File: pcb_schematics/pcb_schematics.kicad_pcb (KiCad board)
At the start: 2 copper layers, 140 x 108 mm, 56 parts, among them J1 CUE_SJ1-352XNG, J2 Conn_01x01_Pin, SW1 SW_Push, SW2 SW_Push, SW3 SW_Push, SW4 SW_Push, SW5 RotaryEncoder, SW6 RotaryEncoder, U1 RPi_Pico_TH, U2 RDA5807M_Module, U3 LM386, U4 LM386

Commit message: Pcb (#1)
* Converted to connectors

* Updates PCb according to ROB's feedback

Added PCb layour according to the discussion with butoons and display on top and display below using front copper. Added Radio module using back copper. Speakers left to set up using back copper.

* compeltes PCB

Only the DRC has a couple errors

* Updates footprints in schematic

* Fixes errors in DRC

Adds SMD capacitors too

* Runs DRC and ERC again

* Accomodating usb cable

* Revision 3

Changed the amplifier and the rotary encoder schemtic. Needs work on pcb

* completes third version of PCB

* fixed issues mentioned by rob and brent

Fix iteration 1

* made changes based on changes requested

Fix iteration 2

* Submitted to JLCPCB

Modification with pcb_schematics being the final version.
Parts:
- removed C17, C18, C19, C20, C21, C22, C23, C24, C25, C26, C27, C28, C29, C30, C31, C32: 10 nF, Capacitor_THT:CP_Radial_D4.0mm_P1.50mm
- removed SW2, SW3, SW4: SW_Push, Button_Switch_THT:Push_E-Switch_KS01Q01
- removed SW5, SW6: RotaryEncoder, Rotary_Encoder:RotaryEncoder_Alps_EC11E-Switch_Vertical_H20mm
- added H1: MountingHole, MountingHole:MountingHole_3.2mm_M3, F.Cu at (100.0, 48.0)
- added H2: MountingHole, MountingHole:MountingHole_3.2mm_M3, F.Cu at (190.0, 48.0)
- added H3: MountingHole, MountingHole:MountingHole_3.2mm_M3, F.Cu at (190.0, 138.0)
- added H4: MountingHole, MountingHole:MountingHole_3.2mm_M3, F.Cu at (100.0, 138.0)
- added J3: Conn_01x05, Connector_PinHeader_2.54mm:PinHeader_1x05_P2.54mm_Vertical, F.Cu at (176.5, 45.3)
- added J4: Conn_01x05, Connector_PinHeader_2.54mm:PinHeader_1x05_P2.54mm_Vertical, F.Cu at (149.0, 45.3)
- added J5: Conn_01x05, Connector_PinHeader_2.54mm:PinHeader_1x05_P2.54mm_Vertical, F.Cu at (123.0, 45.8)
- added R10: 10Ω, Resistor_THT:R_Axial_DIN0207_L6.3mm_D2.5mm_P10.16mm_Horizontal, F.Cu at (177.0, 60.0)
- added R5: 10Ω, Resistor_THT:R_Axial_DIN0207_L6.3mm_D2.5mm_P10.16mm_Horizontal, F.Cu at (156.5, 49.0)
- added R6: 10Ω, Resistor_THT:R_Axial_DIN0207_L6.3mm_D2.5mm_P10.16mm_Horizontal, F.Cu at (140.0, 57.3)
- added R7: 10kΩ, Resistor_THT:R_Axial_DIN0207_L6.3mm_D2.5mm_P10.16mm_Horizontal, F.Cu at (129.0, 55.0)
- added R8: 10kΩ, Resistor_THT:R_Axial_DIN0207_L6.3mm_D2.5mm_P10.16mm_Horizontal, F.Cu at (121.0, 65.0)
- added R9: 10Ω, Resistor_THT:R_Axial_DIN0207_L6.3mm_D2.5mm_P10.16mm_Horizontal, F.Cu at (169.0, 49.0)
- added R_Pullup1: 10kΩ, Resistor_THT:R_Axial_DIN0207_L6.3mm_D2.5mm_P10.16mm_Horizontal, F.Cu at (153.0, 51.0)
- added R_Pullup2: 10kΩ, Resistor_THT:R_Axial_DIN0207_L6.3mm_D2.5mm_P10.16mm_Horizontal, F.Cu at (137.0, 55.0)
- added R_Pullup4: 10kΩ, Resistor_THT:R_Axial_DIN0207_L6.3mm_D2.5mm_P10.16mm_Horizontal, F.Cu at (125.0, 50.0)
- added R_Pullup5: 10kΩ, Resistor_THT:R_Axial_DIN0207_L6.3mm_D2.5mm_P10.16mm_Horizontal, F.Cu at (117.0, 50.0)
- added R_Pullup6: 10kΩ, Resistor_THT:R_Axial_DIN0207_L6.3mm_D2.5mm_P10.16mm_Horizontal, F.Cu at (182.0, 53.0)
- added R_Pullup7: 10kΩ, Resistor_THT:R_Axial_DIN0207_L6.3mm_D2.5mm_P10.16mm_Horizontal, F.Cu at (166.0, 51.0)
- added TP1: TestPoint, TestPoint:TestPoint_Keystone_5000-5004_Miniature, F.Cu at (171.0, 137.0)
- added TP10: TestPoint, TestPoint:TestPoint_Keystone_5000-5004_Miniature, B.Cu at (184.0, 106.3)
- added TP11: TestPoint, TestPoint:TestPoint_Keystone_5000-5004_Miniature, B.Cu at (186.0, 84.0)
- added TP12: TestPoint, TestPoint:TestPoint_Keystone_5000-5004_Miniature, B.Cu at (186.0, 71.0)
- added TP13: TestPoint, TestPoint:TestPoint_Keystone_5000-5004_Miniature, B.Cu at (188.0, 116.0)
- added TP14: TestPoint, TestPoint:TestPoint_Keystone_5000-5004_Miniature, F.Cu at (182.0, 48.3)
- added TP15: TestPoint, TestPoint:TestPoint_Keystone_5000-5004_Miniature, F.Cu at (163.0, 49.0)
- added TP16: TestPoint, TestPoint:TestPoint_Keystone_5000-5004_Miniature, F.Cu at (129.0, 51.0)
- added TP17: TestPoint, TestPoint:TestPoint_Keystone_5000-5004_Miniature, F.Cu at (113.0, 47.0)
- added TP18: TestPoint, TestPoint:TestPoint_Keystone_5000-5004_Miniature, F.Cu at (161.0, 54.0)
- added TP19: TestPoint, TestPoint:TestPoint_Keystone_5000-5004_Miniature, F.Cu at (146.0, 51.0)
- added TP2: TestPoint, TestPoint:TestPoint_Keystone_5000-5004_Miniature, F.Cu at (170.0, 122.0)
- added TP3: TestPoint, TestPoint:TestPoint_Keystone_5000-5004_Miniature, F.Cu at (188.0, 124.0)
- added TP4: TestPoint, TestPoint:TestPoint_Keystone_5000-5004_Miniature, B.Cu at (166.0, 121.3)
- added TP5: TestPoint, TestPoint:TestPoint_Keystone_5000-5004_Miniature, B.Cu at (178.0, 106.3)
- added TP6: TestPoint, TestPoint:TestPoint_Keystone_5000-5004_Miniature, B.Cu at (118.0, 90.3)
- added TP7: TestPoint, TestPoint:TestPoint_Keystone_5000-5004_Miniature, B.Cu at (126.0, 118.3)
- added TP8: TestPoint, TestPoint:TestPoint_Keystone_5000-5004_Miniature, B.Cu at (116.0, 128.3)
- added TP9: TestPoint, TestPoint:TestPoint_Keystone_5000-5004_Miniature, B.Cu at (105.0, 100.0)
- C1, C10, C11, C14, C2: value 10 µF -> 0.01 µF; footprint Capacitor_THT:CP_Radial_D5.0mm_P2.00mm -> Capacitor_THT:C_Axial_L3.8mm_D2.6mm_P7.50mm_Horizontal
- C12: value 10 µF -> 0.1 µF; footprint Capacitor_THT:CP_Radial_D5.0mm_P2.00mm -> Capacitor_THT:C_Axial_L3.8mm_D2.6mm_P7.50mm_Horizontal; moved to B.Cu
- C13: value 10 µF -> 0.1 µF; footprint Capacitor_THT:CP_Radial_D5.0mm_P2.00mm -> Capacitor_THT:C_Axial_L3.8mm_D2.6mm_P7.50mm_Horizontal
- C15, C3, C6, R1, R2, Rpullup1, Rpullup2, U2, U3, U4: moved to B.Cu
- C16: value 10 µF -> 470 µF; footprint Capacitor_THT:CP_Radial_D5.0mm_P2.00mm -> Capacitor_THT:CP_Radial_D6.3mm_P2.50mm; moved to B.Cu
- C4, C5: value 10 nF -> 0.05 µF; footprint Capacitor_THT:CP_Radial_D4.0mm_P1.50mm -> Capacitor_THT:C_Axial_L3.8mm_D2.6mm_P7.50mm_Horizontal; moved to B.Cu
- C7, C8: value 10 nF -> 0.1 µF; footprint Capacitor_THT:CP_Radial_D4.0mm_P1.50mm -> Capacitor_SMD:C_0603_1608Metric; moved to B.Cu
- C9: value 470 µF -> 0.01 µF; footprint Capacitor_THT:CP_Radial_D6.3mm_P2.50mm -> Capacitor_THT:C_Axial_L3.8mm_D2.6mm_P7.50mm_Horizontal
- J1: footprint ECE:CUE_SJ1-352XNG -> Connector_PinHeader_2.54mm:PinHeader_1x05_P2.54mm_Vertical; moved to B.Cu
- J2: footprint Connector:Banana_Jack_1Pin -> Connector_Pin:Pin_D1.0mm_L10.0mm_LooseFit
- LS1, LS2: footprint ECE:CUE_CMA-4544PF-W -> TerminalBlock_Phoenix:TerminalBlock_Phoenix_MKDS-1,5-2_1x02_P5.00mm_Horizontal; moved to B.Cu
- R3, R4: value 10Ω -> 10 k
- RV1, RV2: footprint ECE:Bourns_PTV09_Horiz -> Connector_PinHeader_2.54mm:PinHeader_1x03_P2.54mm_Vertical; moved to B.Cu
- R_Pullup3: value 2kΩ -> 10kΩ
- SW1: footprint Button_Switch_THT:Push_E-Switch_KS01Q01 -> Connector_PinHeader_2.54mm:PinHeader_1x02_P2.54mm_Vertical
- moved DISP1 182.1 mm to (224.9, 142.4), turned to 90 degrees
- moved LS1 87.0 mm to (100.0, 127.0), turned to 90 degrees
- moved SW1 83.5 mm to (184.0, 110.0), turned to 90 degrees
- moved U3 82.6 mm to (116.0, 118.3), turned to 180 degrees
- moved U2 68.0 mm to (173.1, 95.2)
- moved C3 67.5 mm to (100.0, 95.0), turned to 180 degrees
- moved C6 64.3 mm to (110.0, 133.0), turned to 180 degrees
- moved C13 62.8 mm to (105.2, 108.0)
- moved J2 62.7 mm to (182.0, 83.3)
- moved C12 59.9 mm to (103.0, 86.5), turned to 90 degrees
- moved U1 58.7 mm to (148.1, 117.6)
- moved C5 58.0 mm to (113.2, 136.3)
- moved C9 55.7 mm to (160.0, 57.0), turned to -90 degrees
- moved U4 54.7 mm to (111.0, 70.8), turned to 180 degrees
- moved R2 52.4 mm to (121.2, 140.3), turned to 180 degrees
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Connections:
- C1 pad 1: Net-(U3-BYPASS) -> /ROT3A
- C10 pad 1: Net-(C10-Pad1) -> GND
- C10 pad 2: Net-(C10-Pad2) -> /ROT1A
- C11 pad 1: Net-(C10-Pad2) -> GND
- C11 pad 2: Net-(C11-Pad2) -> /ROT2B
- C12 pad 1: Net-(C10-Pad1) -> GND
- C12 pad 2: Net-(C11-Pad2) -> +5V
- C13 pad 1: Net-(C13-Pad1) -> GND
- C13 pad 2: Net-(C13-Pad2) -> +5V
- C14 pad 1: Net-(C13-Pad1) -> GND
- C14 pad 2: Net-(C14-Pad2) -> /ROT3B
- C15 pad 2: Net-(C14-Pad2) -> Net-(U3-+)
- C16 pad 1: Net-(C13-Pad2) -> Net-(C16-Pad1)
- C16 pad 2: Net-(C14-Pad2) -> Net-(U4-+)
- C2 pad 1: GND -> /ROT2A
- C2 pad 2: Net-(U4-BYPASS) -> GND
- C3 pad 1: Net-(C10-Pad1) -> Net-(C3-Pad1)
- C4 pad 1: Net-(C17-Pad1) -> Net-(C3-Pad1)
- C4 pad 2: Net-(C10-Pad1) -> Net-(C4-Pad2)
- C5 pad 1: Net-(C21-Pad1) -> Net-(C5-Pad1)
- C5 pad 2: Net-(C13-Pad1) -> Net-(C5-Pad2)
- C6 pad 1: Net-(C13-Pad1) -> Net-(C5-Pad1)
- C6 pad 2: Net-(C15-Pad1) -> Net-(C6-Pad2)
- C7 pad 1: Net-(C25-Pad1) -> GND
- C7 pad 2: /ROUT -> +5V
- C8 pad 1: Net-(C29-Pad1) -> GND
- C8 pad 2: /LOUT -> +5V
- C9 pad 1: Net-(C3-Pad2) -> /ROT1B
- C9 pad 2: Net-(C11-Pad2) -> GND
- J1 pad 2: /RSpeaker -> /LOUT
- J1 pad 3: /LSpeaker -> /ROUT
- J1 pad 4: /LOUT -> /RSpeaker
- J1 pad 5: /ROUT -> /LSpeaker
- LS1 pad 1: Net-(C14-Pad2) -> Net-(C6-Pad2)
- LS2 pad 1: Net-(C11-Pad2) -> Net-(C3-Pad2)
- R1 pad 1: Net-(C17-Pad1) -> Net-(C4-Pad2)
- R2 pad 1: Net-(C21-Pad1) -> Net-(C5-Pad2)
- R3 pad 1: Net-(C25-Pad1) -> Net-(R3-Pad1)
- R3 pad 2: GND -> /LSpeaker
- R4 pad 1: Net-(C29-Pad1) -> /RSpeaker
- R4 pad 2: GND -> Net-(R4-Pad2)
- RV1 pad 1: /LSpeaker -> Net-(R3-Pad1)
- RV1 pad 2: Net-(U3-+) -> Net-(C15-Pad1)
- RV2 pad 1: /RSpeaker -> Net-(R4-Pad2)
- RV2 pad 2: Net-(U4-+) -> Net-(C16-Pad1)
- U1 pad 10: unconnected-(U1-GP7-Pad10) -> /ROT2B
- U1 pad 2: unconnected-(U1-GP1-Pad2) -> /SW2
- U1 pad 31: unconnected-(U1-GP26/ADC0-Pad31) -> /SW3
- U1 pad 32: /RotB -> /ROT3B
- U1 pad 34: /RotA -> /ROT3A
- U1 pad 4: /SW2 -> /ROT1B
- U1 pad 5: unconnected-(U1-GP3-Pad5) -> /ROT1A
- U1 pad 6: /SW3 -> unconnected-(U1-GP4-Pad6)
- U1 pad 7: unconnected-(U1-GP5-Pad7) -> /SW4
- U1 pad 9: /SW4 -> /ROT2A
- U3 pad 5: Net-(C13-Pad1) -> Net-(C5-Pad1)
- U3 pad 6: /3V3 -> +5V
- U3 pad 7: Net-(U3-BYPASS) -> unconnected-(U3-BYPASS-Pad7)
- U4 pad 5: Net-(C10-Pad1) -> Net-(C3-Pad1)
- U4 pad 6: /3V3 -> +5V
- U4 pad 7: Net-(U4-BYPASS) -> unconnected-(U4-BYPASS-Pad7)
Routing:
- net Net-(U3-+): track 240.0 -> 10.2 mm, vias 1 -> 0
- net +5V: track 0.00 -> 162.8 mm, vias 0 -> 1
- net /CS: track 163.9 -> 63.1 mm, vias 0 -> 1
- net Net-(C10-Pad1): track 94.9 -> 0.00 mm, vias 2 -> 0
- net /I2CSCK: track 176.6 -> 83.6 mm
- net Net-(R3-Pad1): track 0.00 -> 91.7 mm
- net /I2CTX: track 153.2 -> 70.5 mm, vias 0 -> 4
- net Net-(R4-Pad2): track 0.00 -> 82.6 mm
- net Net-(C11-Pad2): track 82.1 -> 0.00 mm, vias 1 -> 0
- net /ROUT: track 89.0 -> 18.2 mm, vias 3 -> 0
- net /RSpeaker: track 81.8 -> 14.0 mm
- net Net-(C29-Pad1): track 66.7 -> 0.00 mm
- net /ROT3B: track 0.00 -> 63.7 mm
- net /ROT2B: track 0.00 -> 61.5 mm
- net /ROT3A: track 0.00 -> 58.9 mm
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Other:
- board size 140 x 108 mm -> 100 x 100 mm
- board text added: "Antenna"
- board text added: "Clock-Radio 29-06-25 Animish Murthy, Krishna Gupta 007, MI6"

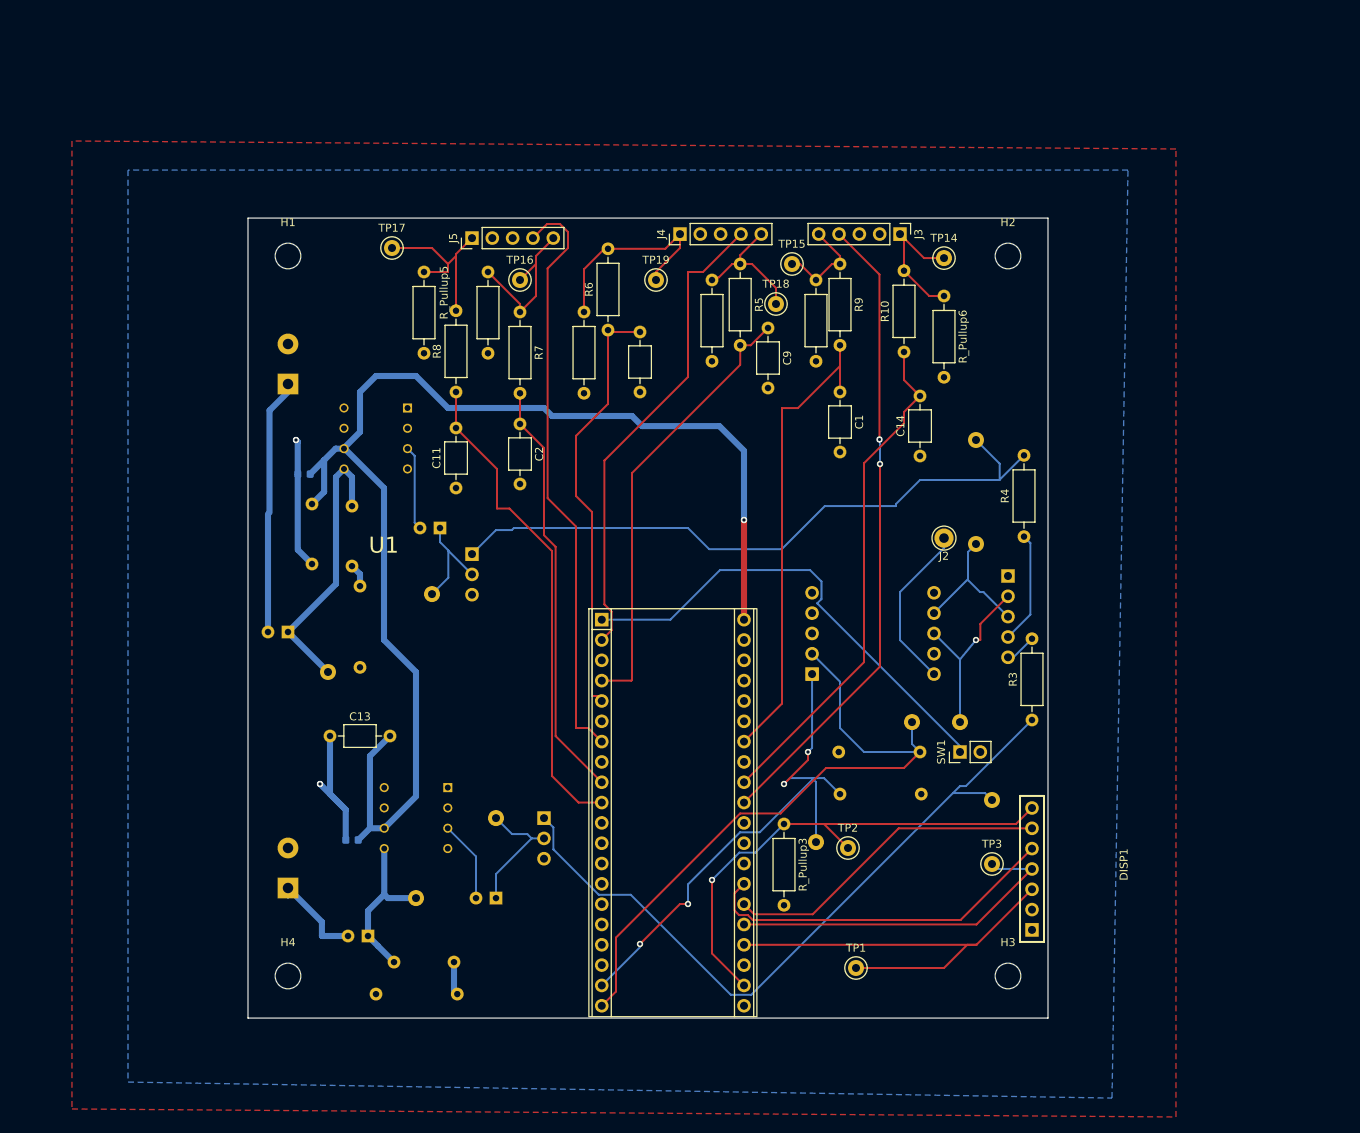
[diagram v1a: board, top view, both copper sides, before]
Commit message: Runs DRC and ERC again
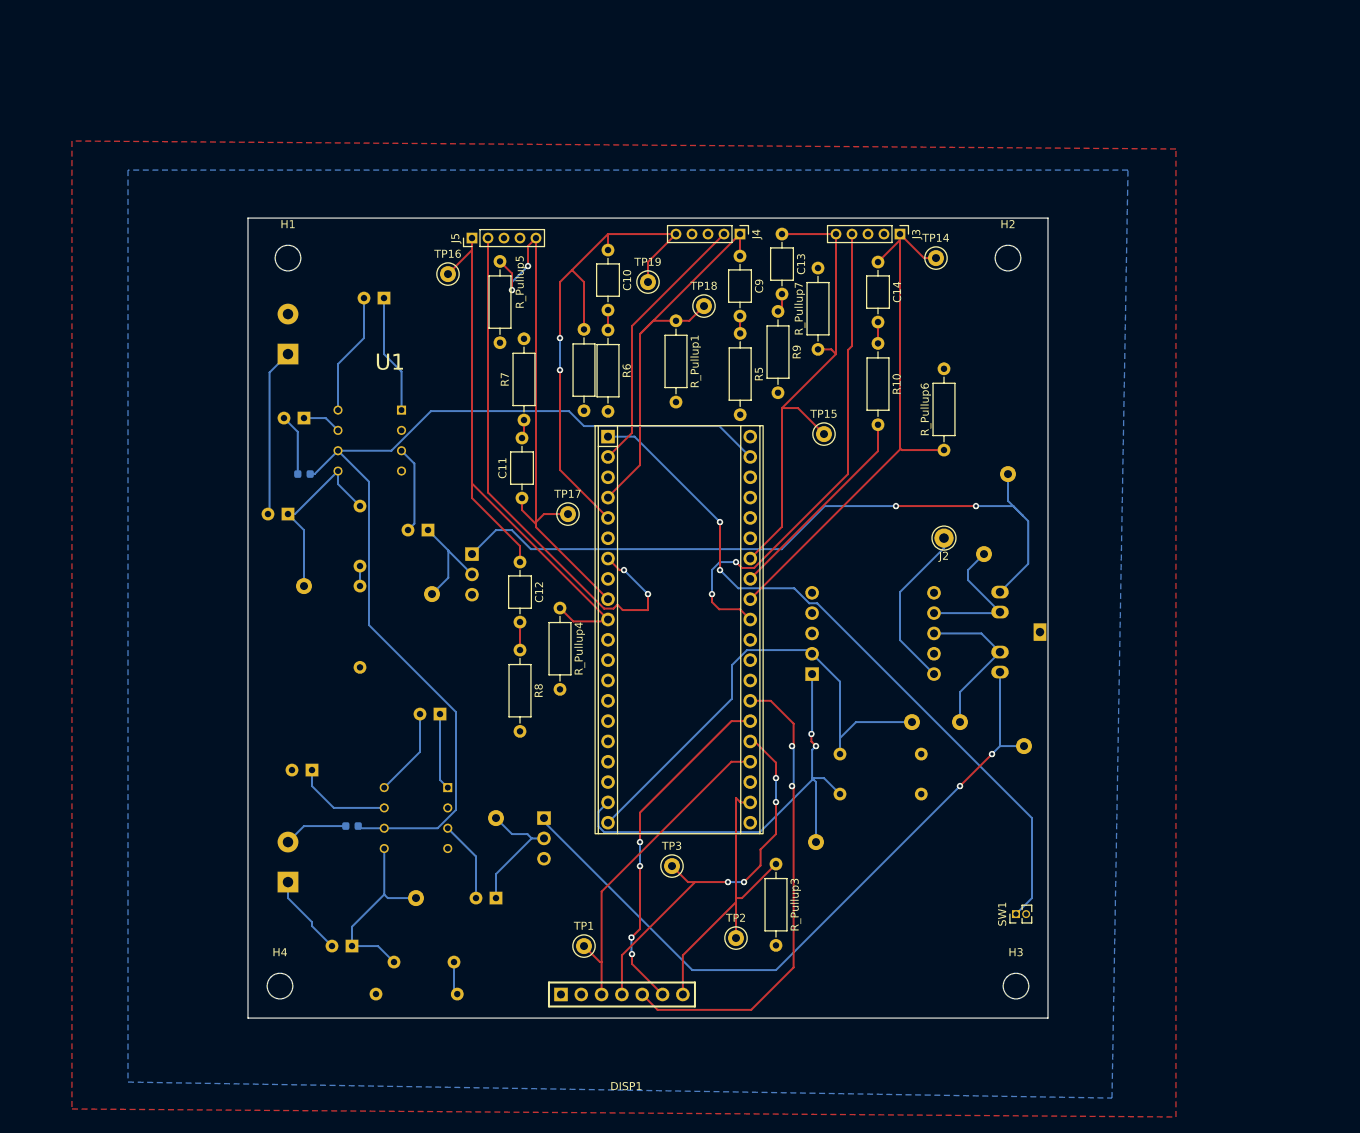
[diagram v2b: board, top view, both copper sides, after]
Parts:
- removed R3, R4: 10 k, Resistor_THT:R_Axial_DIN0207_L6.3mm_D2.5mm_P10.16mm_Horizontal
- added C17: 10 µF, Capacitor_THT:CP_Radial_D6.3mm_P2.50mm, B.Cu at (119.0, 105.3)
- added C18: 10 µF, Capacitor_THT:CP_Radial_D6.3mm_P2.50mm, B.Cu at (112.0, 53.3)
- C1, C2: value 0.01 µF -> 10 µF; footprint Capacitor_THT:C_Axial_L3.8mm_D2.6mm_P7.50mm_Horizontal -> Capacitor_THT:CP_Radial_D6.3mm_P2.50mm; moved to B.Cu
- C10, C11, C14, C9: value 0.01 µF -> 0.05 µF
- C12: value 0.1 µF -> 0.05 µF; moved to F.Cu
- C13: value 0.1 µF -> 0.05 µF
- J1: value CUE_SJ1-352XNG -> Jack; footprint Connector_PinHeader_2.54mm:PinHeader_1x05_P2.54mm_Vertical -> ECE:CUE_SJ1-352XNG
- J3, J4, J5: footprint Connector_PinHeader_2.54mm:PinHeader_1x05_P2.54mm_Vertical -> Connector_PinHeader_2.00mm:PinHeader_1x05_P2.00mm_Vertical
- R7, R8: value 10kΩ -> 10Ω
- R_Pullup1, R_Pullup2, R_Pullup3, R_Pullup4, R_Pullup5, R_Pullup6, R_Pullup7: value 10kΩ -> 2kΩ
- SW1: footprint Connector_PinHeader_2.54mm:PinHeader_1x02_P2.54mm_Vertical -> Connector_PinHeader_1.27mm:PinHeader_1x02_P1.27mm_Vertical
- moved DISP1 105.3 mm to (124.0, 172.3), turned to 0 degrees
- moved C13 84.4 mm to (161.8, 45.3), turned to -90 degrees
- moved C1 81.2 mm to (103.0, 112.3), turned to 180 degrees
- moved R_Pullup4 43.0 mm to (134.0, 92.0)
- moved TP3 40.0 mm to (148.0, 124.3)
- moved TP17 39.9 mm to (135.0, 80.3)
- moved TP1 34.1 mm to (137.0, 134.3)
- moved R8 33.2 mm to (129.0, 97.3), turned to -90 degrees
- moved C2 27.0 mm to (102.0, 68.3), turned to 180 degrees
- moved C12 26.0 mm to (129.0, 86.3), turned to -90 degrees
- moved C14 24.8 mm to (173.8, 48.8), turned to -90 degrees
- moved U1 22.9 mm to (148.9, 94.7)
- moved TP15 21.6 mm to (167.0, 70.3)
- moved SW1 21.4 mm to (191.0, 130.3)
- moved R_Pullup6 19.3 mm to (182.0, 72.3), turned to 90 degrees
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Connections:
- C1 pad 1: /ROT3A -> Net-(U3-BYPASS)
- C10 pad 1: GND -> /ROT1A
- C10 pad 2: /ROT1A -> Net-(C10-Pad2)
- C11 pad 1: GND -> /ROT2A
- C11 pad 2: /ROT2B -> Net-(C11-Pad2)
- C12 pad 1: GND -> /ROT2B
- C12 pad 2: +5V -> Net-(C12-Pad2)
- C13 pad 1: GND -> /ROT3A
- C13 pad 2: +5V -> Net-(C13-Pad2)
- C14 pad 1: GND -> /ROT3B
- C14 pad 2: /ROT3B -> Net-(C14-Pad2)
- C2 pad 1: /ROT2A -> Net-(U4-BYPASS)
- C7 pad 2: +5V -> 5V
- C8 pad 2: +5V -> 5V
- C9 pad 2: GND -> Net-(C9-Pad2)
- J1 pad 2: /LOUT -> /RSpeaker
- J1 pad 3: /ROUT -> /LSpeaker
- J1 pad 4: /RSpeaker -> /ROUT
- J1 pad 5: /LSpeaker -> /LOUT
- J3 pad 1: Net-(J3-Pin_1) -> /ROT3B
- J3 pad 5: Net-(J3-Pin_5) -> /ROT3A
- J4 pad 1: Net-(J4-Pin_1) -> /ROT1B
- J4 pad 2: GND -> /SW2
- J4 pad 4: /SW2 -> GND
- J4 pad 5: Net-(J4-Pin_5) -> /ROT1A
- J5 pad 1: Net-(J5-Pin_1) -> /ROT2B
- J5 pad 2: GND -> /SW4
- J5 pad 4: /SW4 -> GND
- J5 pad 5: Net-(J5-Pin_5) -> /ROT2A
- R10 pad 1: /ROT3B -> Net-(C14-Pad2)
- R10 pad 2: Net-(J3-Pin_1) -> GND
- R5 pad 1: Net-(J4-Pin_5) -> Net-(C9-Pad2)
- R5 pad 2: /ROT1B -> GND
- R6 pad 1: /ROT1A -> Net-(C10-Pad2)
- R6 pad 2: Net-(J4-Pin_1) -> GND
- R7 pad 1: Net-(J5-Pin_5) -> Net-(C11-Pad2)
- R7 pad 2: /ROT2A -> GND
- R8 pad 1: /ROT2B -> Net-(C12-Pad2)
- R8 pad 2: Net-(J5-Pin_1) -> GND
- R9 pad 1: Net-(J3-Pin_5) -> Net-(C13-Pad2)
- R9 pad 2: /ROT3A -> GND
- RV1 pad 1: Net-(R3-Pad1) -> /LSpeaker
- RV2 pad 1: Net-(R4-Pad2) -> /RSpeaker
- R_Pullup1 pad 1: Net-(J4-Pin_5) -> /ROT1B
- R_Pullup2 pad 1: Net-(J4-Pin_1) -> /ROT1A
- R_Pullup4 pad 1: Net-(J5-Pin_5) -> /ROT2B
- R_Pullup5 pad 1: Net-(J5-Pin_1) -> /ROT2A
- R_Pullup6 pad 1: Net-(J3-Pin_1) -> /ROT3B
- R_Pullup7 pad 1: Net-(J3-Pin_5) -> /ROT3A
- TP12 pad 1: Net-(R4-Pad2) -> /RSpeaker
- TP13 pad 1: Net-(R3-Pad1) -> /LSpeaker
- TP14 pad 1: Net-(J3-Pin_1) -> /ROT3B
- TP15 pad 1: Net-(J3-Pin_5) -> /ROT3A
- TP16 pad 1: Net-(J5-Pin_5) -> /ROT2B
- TP17 pad 1: Net-(J5-Pin_1) -> /ROT2A
- TP18 pad 1: Net-(J4-Pin_5) -> /ROT1B
- TP19 pad 1: Net-(J4-Pin_1) -> /ROT1A
- U1 pad 39: unconnected-(U1-VSYS-Pad39) -> 5V
- U3 pad 1: unconnected-(U3-GAIN-Pad1) -> Net-(C17-Pad1)
- U3 pad 6: +5V -> 5V
- U3 pad 7: unconnected-(U3-BYPASS-Pad7) -> Net-(U3-BYPASS)
- U3 pad 8: unconnected-(U3-GAIN-Pad8) -> Net-(C17-Pad2)
- U4 pad 1: unconnected-(U4-GAIN-Pad1) -> Net-(C18-Pad1)
- U4 pad 6: +5V -> 5V
- U4 pad 7: unconnected-(U4-BYPASS-Pad7) -> Net-(U4-BYPASS)
- U4 pad 8: unconnected-(U4-GAIN-Pad8) -> Net-(C18-Pad2)
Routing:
- net +5V: track 162.8 -> 0.00 mm, vias 1 -> 0
- net 5V: track 0.00 -> 124.9 mm
- net Net-(R3-Pad1): track 91.7 -> 0.00 mm
- net /LSpeaker: track 3.96 -> 89.0 mm, vias 0 -> 2
- net Net-(R4-Pad2): track 82.6 -> 0.00 mm
- net /RSpeaker: track 14.0 -> 91.0 mm, vias 0 -> 2
- net /SW1: track 59.9 -> 89.1 mm, vias 0 -> 2
- net /SW2: track 59.8 -> 33.9 mm
- net Net-(J4-Pin_1): track 25.7 -> 0.00 mm
- net Net-(J5-Pin_1): track 23.9 -> 0.00 mm
- net /CS: track 63.1 -> 41.1 mm, vias 1 -> 0
- net /I2CSCK: track 83.6 -> 62.9 mm
- net Net-(J5-Pin_5): track 20.4 -> 0.00 mm
- net Net-(J3-Pin_1): track 18.6 -> 0.00 mm
- net /ROT2B: track 61.5 -> 79.6 mm
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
